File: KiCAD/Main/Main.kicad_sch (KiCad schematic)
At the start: 2 parts, among them J7 Conn_02x05_Top_Bottom_Mountin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

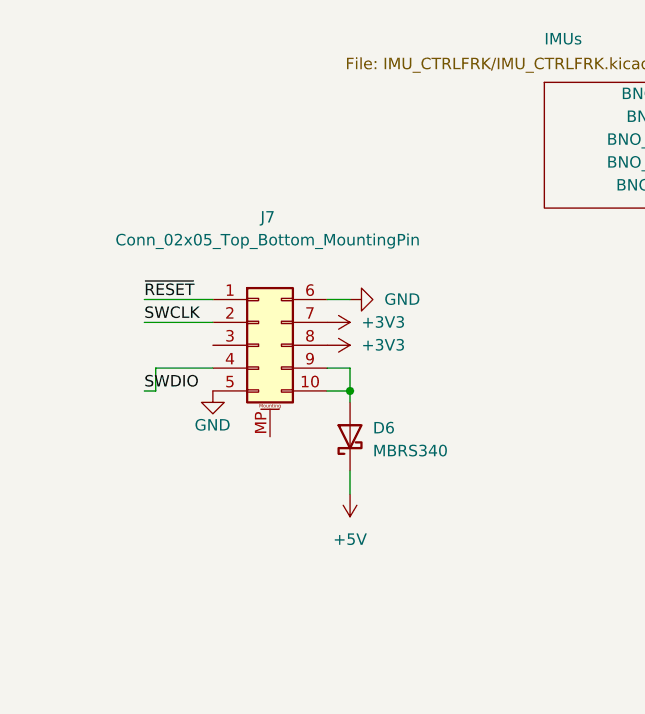
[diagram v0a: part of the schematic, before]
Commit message: Changed out conenctor footprint for smaller, vertical THT component
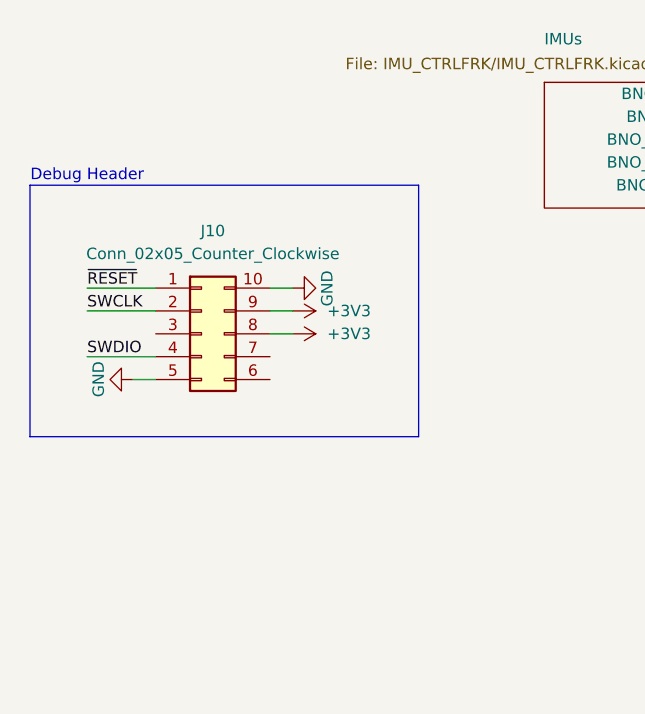
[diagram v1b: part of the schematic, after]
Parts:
- removed D6: MBRS340, Diode_SMD:D_SMC, symbol Diode:MBRS340
- removed J7: Conn_02x05_Top_Bottom_MountingPin, Connector_IDC:IDC-Header_2x05_P2.54mm_Horizontal, symbol Connector_Generic_MountingPin:Conn_02x05_Top_Bottom_MountingPin
- added J10: Conn_02x05_Counter_Clockwise, Connector_PinHeader_2.54mm:PinHeader_2x05_P2.54mm_Vertical, symbol Connector_Generic:Conn_02x05_Counter_Clockwise
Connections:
- net +3V3: now also J10.8 (Pin_8), J10.9 (Pin_9)
- net GND: now also J10.10 (Pin_10), J10.5 (Pin_5)
- net SWCLK: now also J10.2 (Pin_2)
- net SWDIO: now also J10.4 (Pin_4)
- net ~{RESET}: now also J10.1 (Pin_1)
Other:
- note added: "Debug Header"

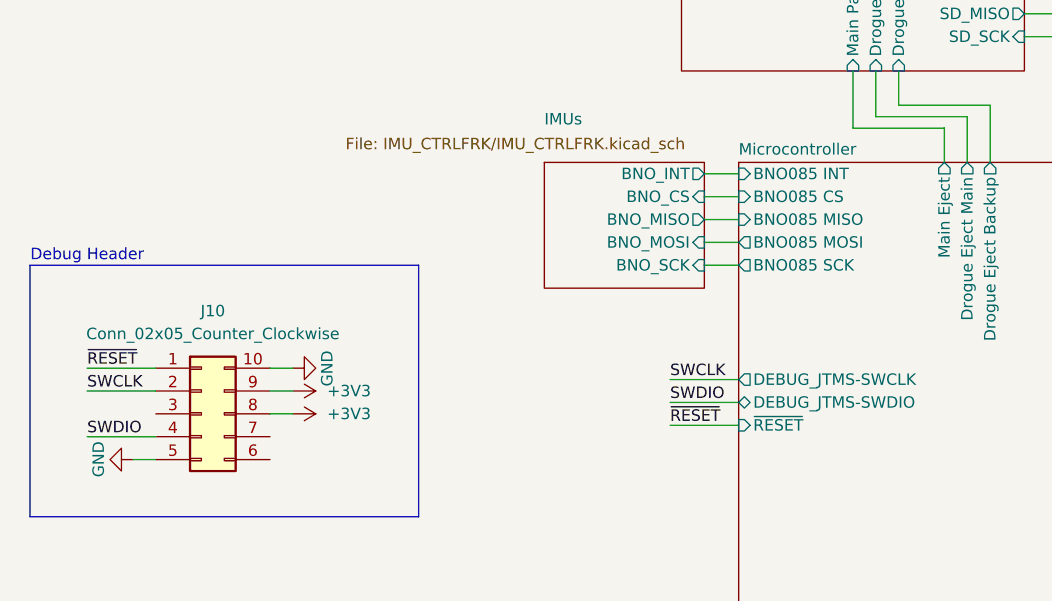
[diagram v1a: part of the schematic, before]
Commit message: Moved around some more pins for easier routing
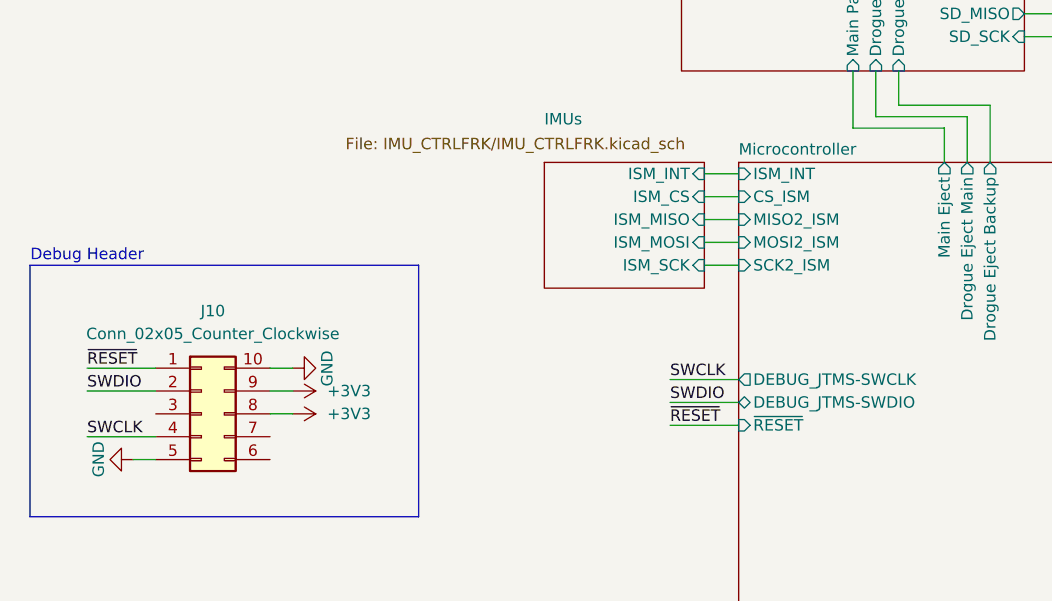
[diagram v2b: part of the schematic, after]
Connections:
- net SWCLK: now also J10.4 (Pin_4); no longer J10.2 (Pin_2)
- net SWDIO: now also J10.2 (Pin_2); no longer J10.4 (Pin_4)
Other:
- sheet IMUs ports: added ISM_CS, ISM_INT, ISM_MISO, ISM_MOSI, ISM_SCK; removed BNO_CS, BNO_INT, BNO_MISO, BNO_MOSI, BNO_SCK
- sheet Microcontroller ports: added CS_ISM, ISM_INT, MISO2_ISM, MOSI2_ISM, SCK2_ISM; removed BNO085 CS, BNO085 INT, BNO085 MISO, BNO085 MOSI, BNO085 SCK
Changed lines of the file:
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@@
 		)
 	)
-	(label "SWCLK"
+	(label "SWDIO"
 		(at 34.29 91.44 0)
-		(effects
-			(font
-				(size 1.27 1.27)
-			)
-			(justify left bottom)
-		)
-	)
-	(label "SWDIO"
-		(at 34.29 96.52 0)
 		(effects
 			(font
@@
 	(label "SWDIO"
 		(at 99.06 92.71 0)
+		(effects
+			(font
+				(size 1.27 1.27)
+			)
+			(justify left bottom)
+		)
+	)
+	(label "SWCLK"
+		(at 34.29 96.52 0)
 		(effects
 			(font
@@
 			)
 		)
-		(pin "BNO085 CS" input
-			(at 106.68 69.85 180)
-			(effects
-				(font
-					(size 1.27 1.27)
-				)
-				(justify left)
-			)
-		)
-		(pin "BNO085 SCK" output
-			(at 106.68 77.47 180)
-			(effects
-				(font
-					(size 1.27 1.27)
-				)
-				(justify left)
-			)
-		)
 		(pin "GPS SCL" output
 			(at 168.91 140.97 0)
@@
 			)
 		)
-		(pin "BNO085 INT" input
-			(at 106.68 67.31 180)
-			(effects
-				(font
-					(size 1.27 1.27)
-				)
-				(justify left)
-			)
-		)
 		(pin "Radio AUX" input
 			(at 106.68 154.94 180)
@@
 			)
 		)
-		(pin "BNO085 MISO" input
-			(at 106.68 72.39 180)
-			(effects
-				(font
-					(size 1.27 1.27)
-				)
-				(justify left)
-			)
-		)
 		(pin "BMP390 INT1" input
 			(at 106.68 162.56 180)
@@
 			)
 		)
-		(pin "BNO085 MOSI" output
-			(at 106.68 74.93 180)
-			(effects
-				(font
-					(size 1.27 1.27)
-				)
-				(justify left)
-			)
-		)
 		(pin "DEBUG_JTMS-SWCLK" output
 			(at 106.68 90.17 180)
@@
 		(pin "~{RESET}" input
 			(at 106.68 95.25 180)
+			(effects
+				(font
+					(size 1.27 1.27)
+				)
+				(justify left)
+			)
+		)
+		(pin "CS_ISM" input
+			(at 106.68 69.85 180)
+			(effects
+				(font
+					(size 1.27 1.27)
+				)
+				(justify left)
+			)
+		)
+		(pin "ISM_INT" input
+			(at 106.68 67.31 180)
+			(effects
+				(font
+					(size 1.27 1.27)
+				)
+				(justify left)
+			)
+		)
+		(pin "MISO2_ISM" input
+			(at 106.68 72.39 180)
+			(effects
+				(font
+					(size 1.27 1.27)
+				)
+				(justify left)
+			)
+		)
+		(pin "MOSI2_ISM" input
+			(at 106.68 74.93 180)
+			(effects
+				(font
+					(size 1.27 1.27)
+				)
+				(justify left)
+			)
+		)
+		(pin "SCK2_ISM" input
+			(at 106.68 77.47 180)
 			(effects
 				(font
@@
 			)
 		)
-		(pin "BNO_CS" input
+		(pin "ISM_CS" input
 			(at 102.87 69.85 0)
 			(effects
@@
 			)
 		)
-		(pin "BNO_INT" output
+		(pin "ISM_INT" input
 			(at 102.87 67.31 0)
 			(effects
@@
 			)
 		)
-		(pin "BNO_MISO" output
+		(pin "ISM_MISO" input
 			(at 102.87 72.39 0)
 			(effects
@@
 			)
 		)
-		(pin "BNO_MOSI" input
+		(pin "ISM_MOSI" input
 			(at 102.87 74.93 0)
 			(effects
@@
 			)
 		)
-		(pin "BNO_SCK" input
+		(pin "ISM_SCK" input
 			(at 102.87 77.47 0)
 			(effects

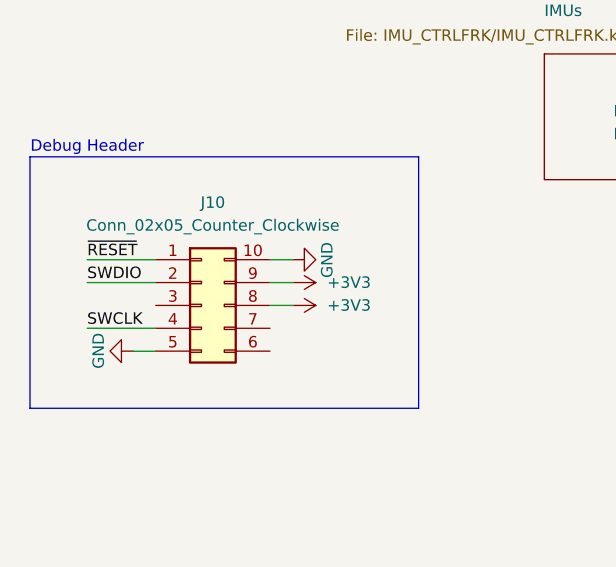
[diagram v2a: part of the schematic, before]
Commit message: Changed debug header out for 2x4 to save space
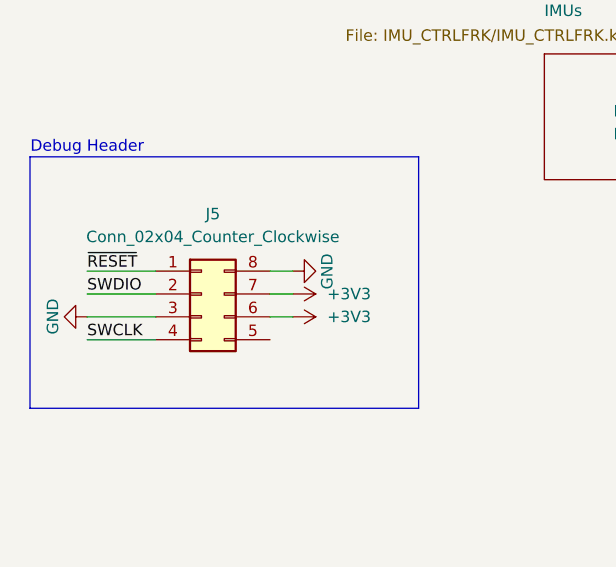
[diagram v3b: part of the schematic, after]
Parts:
- removed J10: Conn_02x05_Counter_Clockwise, Connector_PinHeader_2.54mm:PinHeader_2x05_P2.54mm_Vertical, symbol Connector_Generic:Conn_02x05_Counter_Clockwise
- added J5: Conn_02x04_Counter_Clockwise, Connector_PinHeader_2.54mm:PinHeader_2x04_P2.54mm_Vertical, symbol Connector_Generic:Conn_02x04_Counter_Clockwise
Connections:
- net +3V3: now also J5.6 (Pin_6), J5.7 (Pin_7)
- net GND: now also J5.3 (Pin_3), J5.8 (Pin_8)
- net SWCLK: now also J5.4 (Pin_4)
- net SWDIO: now also J5.2 (Pin_2)
- net ~{RESET}: now also J5.1 (Pin_1)

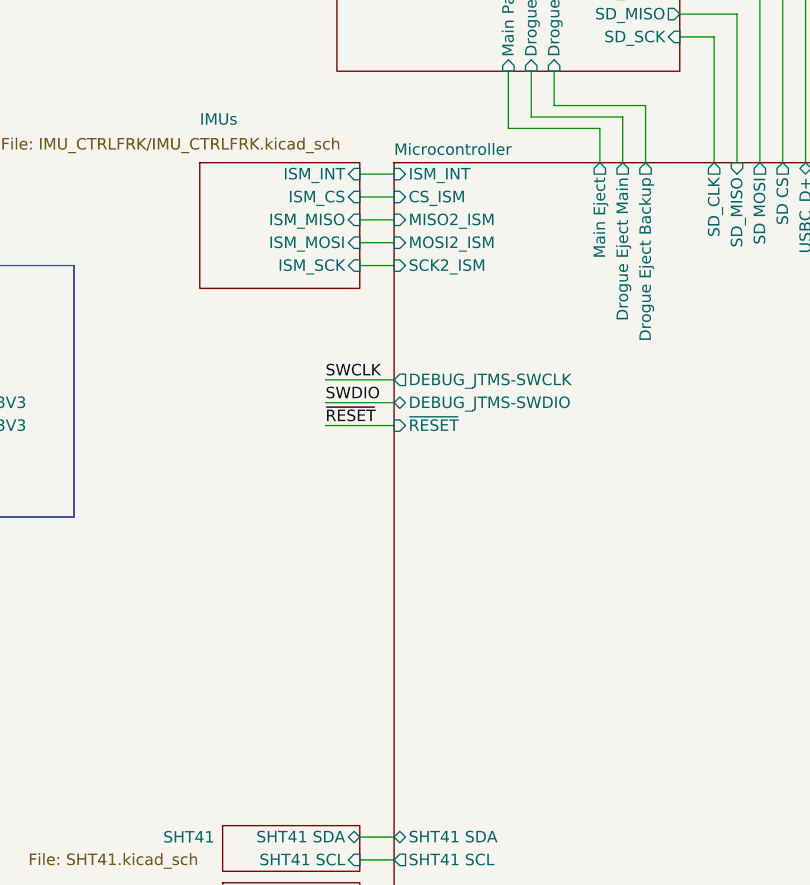
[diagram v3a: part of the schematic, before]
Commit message: Changed BMM350 for LIS2MDL
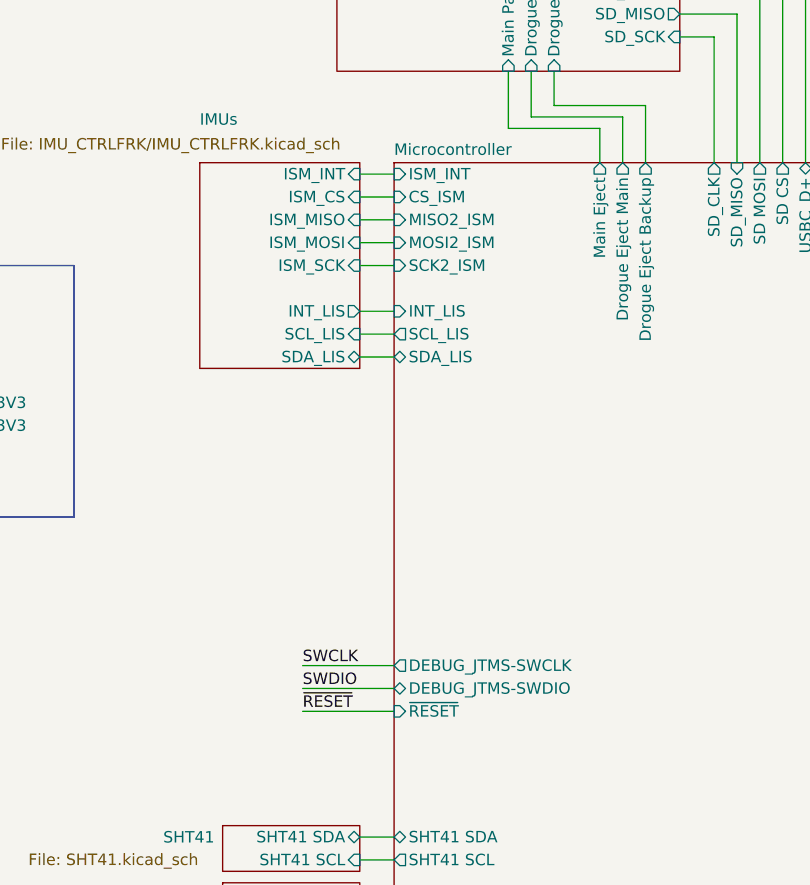
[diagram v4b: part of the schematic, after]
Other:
- sheet IMUs ports: added INT_LIS, SCL_LIS, SDA_LIS; removed none
- sheet Microcontroller ports: added INT_LIS, SCL_LIS, SDA_LIS; removed none
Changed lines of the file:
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@@
 	(wire
 		(pts
-			(xy 99.06 90.17) (xy 106.68 90.17)
+			(xy 96.52 121.92) (xy 106.68 121.92)
 		)
 		(stroke
@@
 	(wire
 		(pts
+			(xy 102.87 85.09) (xy 106.68 85.09)
+		)
+		(stroke
+			(width 0)
+			(type default)
+		)
+	)
+	(wire
+		(pts
 			(xy 102.87 180.34) (xy 106.68 180.34)
 		)
@@
 	(wire
 		(pts
-			(xy 99.06 92.71) (xy 106.68 92.71)
+			(xy 96.52 124.46) (xy 106.68 124.46)
 		)
 		(stroke
@@
 	(wire
 		(pts
-			(xy 99.06 95.25) (xy 106.68 95.25)
+			(xy 96.52 127) (xy 106.68 127)
 		)
 		(stroke
@@
 	(wire
 		(pts
+			(xy 102.87 87.63) (xy 106.68 87.63)
+		)
+		(stroke
+			(width 0)
+			(type default)
+		)
+	)
+	(wire
+		(pts
+			(xy 102.87 82.55) (xy 106.68 82.55)
+		)
+		(stroke
+			(width 0)
+			(type default)
+		)
+	)
+	(wire
+		(pts
 			(xy 102.87 167.64) (xy 106.68 167.64)
 		)
@@
 	)
 	(label "~{RESET}"
-		(at 99.06 95.25 0)
+		(at 96.52 127 0)
 		(effects
 			(font
@@
 	)
 	(label "SWDIO"
-		(at 99.06 92.71 0)
+		(at 96.52 124.46 0)
 		(effects
 			(font
@@
 	)
 	(label "SWCLK"
-		(at 99.06 90.17 0)
+		(at 96.52 121.92 0)
 		(effects
 			(font
@@
 		)
 		(pin "DEBUG_JTMS-SWCLK" output
-			(at 106.68 90.17 180)
+			(at 106.68 121.92 180)
 			(effects
 				(font
@@
 		)
 		(pin "DEBUG_JTMS-SWDIO" bidirectional
-			(at 106.68 92.71 180)
+			(at 106.68 124.46 180)
 			(effects
 				(font
@@
 		)
 		(pin "~{RESET}" input
-			(at 106.68 95.25 180)
+			(at 106.68 127 180)
 			(effects
 				(font
@@
 		(pin "SCK2_ISM" input
 			(at 106.68 77.47 180)
+			(effects
+				(font
+					(size 1.27 1.27)
+				)
+				(justify left)
+			)
+		)
+		(pin "INT_LIS" input
+			(at 106.68 82.55 180)
+			(effects
+				(font
+					(size 1.27 1.27)
+				)
+				(justify left)
+			)
+		)
+		(pin "SCL_LIS" output
+			(at 106.68 85.09 180)
+			(effects
+				(font
+					(size 1.27 1.27)
+				)
+				(justify left)
+			)
+		)
+		(pin "SDA_LIS" bidirectional
+			(at 106.68 87.63 180)
 			(effects
 				(font
@@
 	(sheet
 		(at 85.09 66.04)
-		(size 17.78 13.97)
+		(size 17.78 22.86)
 		(exclude_from_sim no)
 		(in_bom yes)
@@
 			(effects
 				(font
+					(size 1.27 1.27)
+				)
+				(justify right)
+			)
+		)
+		(pin "INT_LIS" output
+			(at 102.87 82.55 0)
+			(effects
+				(font
+					(size 1.27 1.27)
+				)
+				(justify right)
+			)
+		)
+		(pin "SCL_LIS" input
+			(at 102.87 85.09 0)
+			(effects
+				(font
+					(size 1.27 1.27)
+				)
+				(justify right)
+			)
+		)
+		(pin "SDA_LIS" bidirectional
+			(at 102.87 87.63 0)
+			(effects
+				(font

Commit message: Layout and routing
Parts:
- added H1, H2, H3, H4: MountingHole, MountingHole:MountingHole_3.2mm_M3, symbol Mechanical:MountingHole

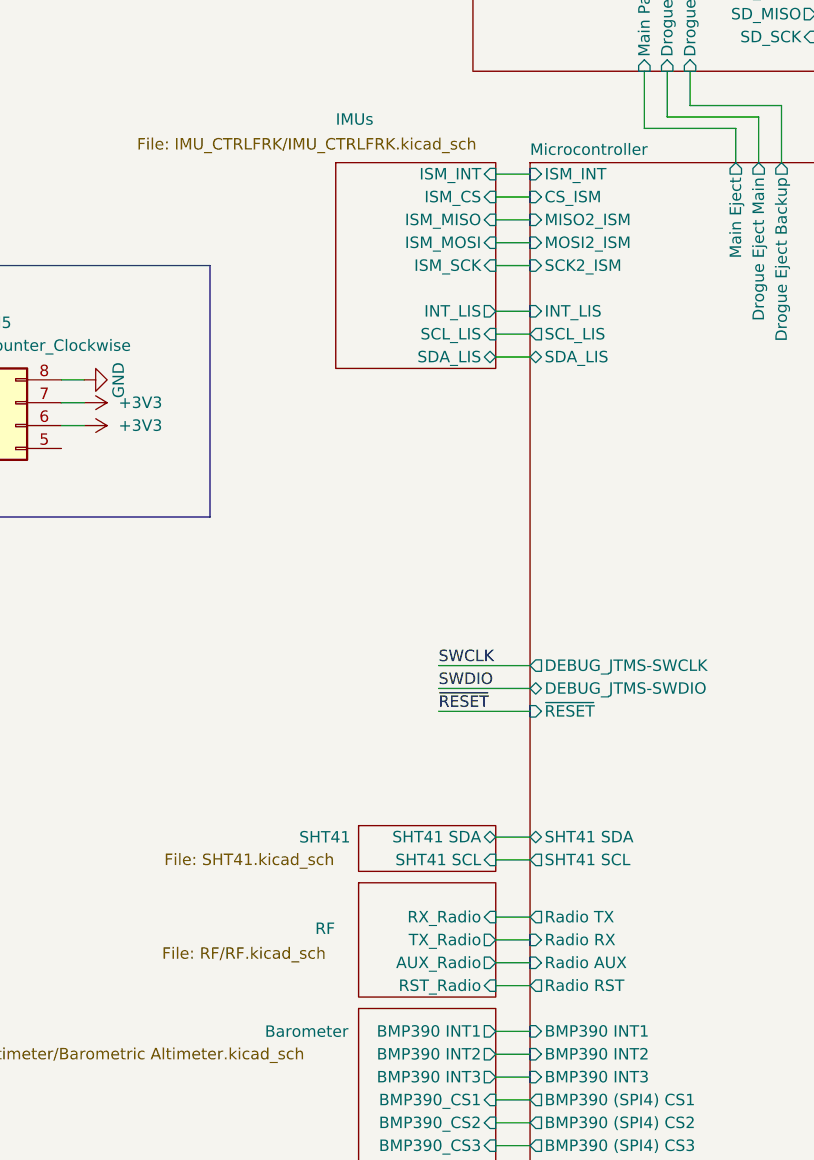
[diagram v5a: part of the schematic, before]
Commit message: Update aux magnetometer, test THs, and silkscreens
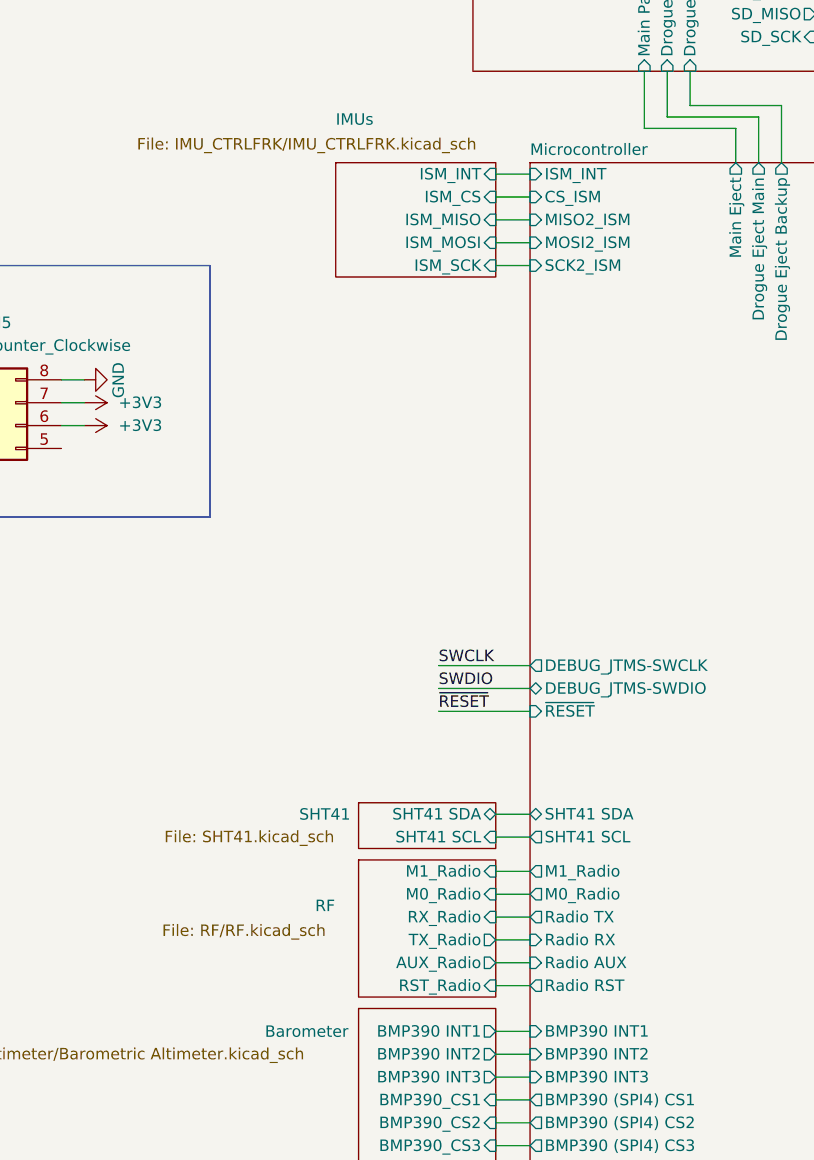
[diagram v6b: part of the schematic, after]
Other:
- sheet IMUs ports: added none; removed INT_LIS, SCL_LIS, SDA_LIS
- sheet Microcontroller ports: added M0_Radio, M1_Radio; removed INT_LIS, SCL_LIS, SDA_LIS
- sheet RF ports: added M0_Radio, M1_Radio; removed none
